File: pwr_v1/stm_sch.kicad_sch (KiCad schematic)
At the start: 2 parts, among them CN11 Conn_02x36_Odd_Even, CN12 Conn_02x36_Odd_Even

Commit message: Schematic updated
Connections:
- net KICKER_DISCHARGE: now also CN12.25 (Pin_25)
- net MOTOR1_ENCODER: now also CN11.9 (Pin_9)
- net MOTOR1_REVERSE: now also CN12.17 (Pin_17)
- net MOTOR2_BREAK: now also CN12.41 (Pin_41)
- net MOTOR3_BREAK: now also CN12.43 (Pin_43)
- net MOTOR3_ENCODER: now also CN12.35 (Pin_35)
- net MOTOR4_REVERSE: now also CN12.47 (Pin_47)
- net SPI_CS_CONF: no longer names the net of CN11.45 (Pin_45)
- net SPI_CS_OUTPUT: no longer names the net of CN11.40 (Pin_40)
- net SPI_CS_RESET: no longer names the net of CN11.39 (Pin_39)
- net SPI_CS_SHIFT: no longer names the net of CN11.43 (Pin_43)
- net SPI_CS_STORE: no longer names the net of CN11.41 (Pin_41)
- net SPI_MOSI: no longer names the net of CN12.29 (Pin_29)
- no-connect marks 112 -> 118
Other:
- moved on the sheet: CN11, CN12

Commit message: Schematic and layout updated
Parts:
- CN11, CN12: footprint (none) -> Connector_PinHeader_2.54mm:PinHeader_2x36_P2.54mm_Vertical_SMD
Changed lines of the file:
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@@
 			)
 		)
-		(property "Footprint" ""
+		(property "Footprint" "Connector_PinHeader_2.54mm:PinHeader_2x36_P2.54mm_Vertical_SMD"
 			(at 91.44 92.71 0)
 			(effects
@@
 			)
 		)
-		(property "Footprint" ""
+		(property "Footprint" "Connector_PinHeader_2.54mm:PinHeader_2x36_P2.54mm_Vertical_SMD"
 			(at 190.5 95.25 0)
 			(effects

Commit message: Schematic updated
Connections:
- net GND: now reaches CN11.20 (Pin_20)
- net 5V: now reaches CN11.6 (Pin_6)
- net MOSI: now reaches CN12.15 (Pin_15)
- net NRF_CSN renamed CS_NRF
- net NRF_MISO renamed MISO
- net NRF_SCK renamed SCK
- no-connect marks 118 -> 115
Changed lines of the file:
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@@
-	)
-	(no_connect
-		(at 99.06 54.61)
 	)
 	(no_connect
@@
 	)
 	(no_connect
-		(at 185.42 69.85)
-	)
-	(no_connect
 		(at 86.36 69.85)
 	)
@@
 	)
 	(no_connect
-		(at 99.06 72.39)
-	)
-	(no_connect
 		(at 185.42 85.09)
 	)
@@
 	(wire
 		(pts
+			(xy 99.06 72.39) (xy 105.918 72.39)
+		)
+		(stroke
+			(width 0)
+			(type default)
+		)
+	)
+	(wire
+		(pts
 			(xy 185.42 95.25) (xy 172.72 95.25)
 		)
@@
 	(wire
 		(pts
+			(xy 172.466 69.85) (xy 185.42 69.85)
+		)
+		(stroke
+			(width 0)
+			(type default)
+		)
+	)
+	(wire
+		(pts
 			(xy 198.12 85.09) (xy 210.82 85.09)
 		)
@@
 		(pts
 			(xy 99.06 105.41) (xy 111.76 105.41)
+		)
+		(stroke
+			(width 0)
+			(type default)
+		)
+	)
+	(wire
+		(pts
+			(xy 99.06 54.61) (xy 105.918 54.61)
 		)
 		(stroke
@@
 		)
 	)
+	(hierarchical_label "5V"
+		(shape input)
+		(at 105.918 54.61 0)
+		(fields_autoplaced yes)
+		(effects
+			(font
+				(size 1.27 1.27)
+			)
+			(justify left)
+		)
+	)
 	(hierarchical_label "MOTOR2_PWM"
 		(shape input)
@@
 		)
 	)
-	(hierarchical_label "NRF_CSN"
+	(hierarchical_label "CS_NRF"
 		(shape input)
 		(at 172.72 54.61 180)
@@
 		)
 	)
+	(hierarchical_label "GND"
+		(shape input)
+		(at 105.918 72.39 0)
+		(fields_autoplaced yes)
+		(effects
+			(font
+				(size 1.27 1.27)
+			)
+			(justify left)
+		)
+	)
 	(hierarchical_label "BTN_USER"
 		(shape input)
@@
 		)
 	)
-	(hierarchical_label "NRF_MISO"
+	(hierarchical_label "MISO"
 		(shape input)
 		(at 172.72 67.31 180)
@@
 		)
 	)
-	(hierarchical_label "NRF_SCK"
+	(hierarchical_label "SCK"
 		(shape input)
 		(at 172.72 64.77 180)
 		(fields_autoplaced yes)
 		(effects
+			(font
+				(size 1.27 1.27)
+			)
+			(justify right)
+		)
+	)
+	(hierarchical_label "MOSI"
+		(shape input)
+		(at 172.466 69.85 180)
+		(fields_autoplaced yes)
+		(effects

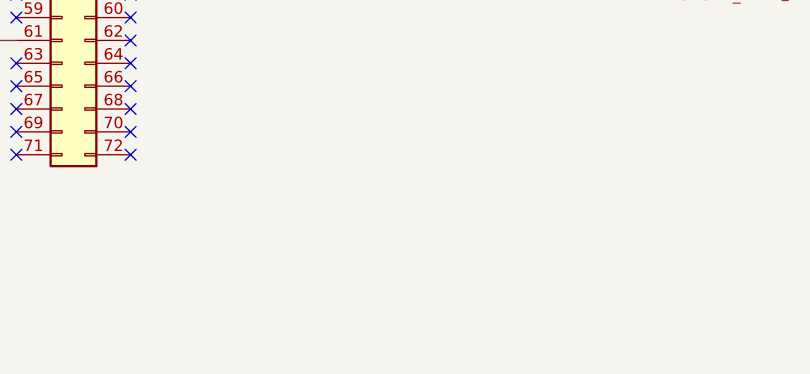
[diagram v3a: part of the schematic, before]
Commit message: Sch and Layout updated; Added batt sup ckt, placed and routed all motor drivers.
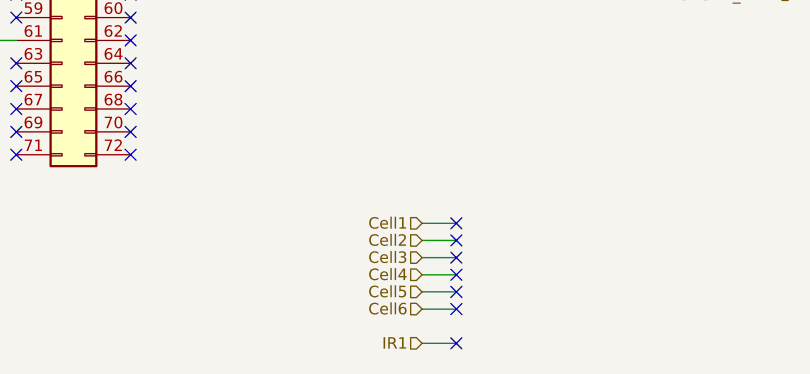
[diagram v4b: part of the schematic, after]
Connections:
- no-connect marks 115 -> 122
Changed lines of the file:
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@@
+	)
+	(no_connect
+		(at 135.255 146.05)
 	)
 	(no_connect
@@
 	)
 	(no_connect
+		(at 135.255 151.765)
+	)
+	(no_connect
 		(at 86.36 87.63)
 	)
@@
 	)
 	(no_connect
+		(at 135.255 147.955)
+	)
+	(no_connect
 		(at 99.06 95.25)
 	)
@@
 	)
 	(no_connect
+		(at 135.255 149.86)
+	)
+	(no_connect
 		(at 185.42 138.43)
 	)
@@
 	)
 	(no_connect
+		(at 135.255 155.575)
+	)
+	(no_connect
 		(at 198.12 128.27)
 	)
@@
 	)
 	(no_connect
+		(at 135.255 159.385)
+	)
+	(no_connect
 		(at 198.12 64.77)
 	)
@@
 	)
 	(no_connect
+		(at 135.255 153.67)
+	)
+	(no_connect
 		(at 198.12 115.57)
 	)
@@
 	(wire
 		(pts
+			(xy 131.445 151.765) (xy 135.255 151.765)
+		)
+		(stroke
+			(width 0)
+			(type default)
+		)
+	)
+	(wire
+		(pts
 			(xy 185.42 67.31) (xy 172.72 67.31)
 		)
@@
 	(wire
 		(pts
+			(xy 131.445 147.955) (xy 135.255 147.955)
+		)
+		(stroke
+			(width 0)
+			(type default)
+		)
+	)
+	(wire
+		(pts
 			(xy 185.42 72.39) (xy 172.72 72.39)
 		)
@@
 	(wire
 		(pts
+			(xy 131.445 159.385) (xy 135.255 159.385)
+		)
+		(stroke
+			(width 0)
+			(type default)
+		)
+	)
+	(wire
+		(pts
 			(xy 99.06 54.61) (xy 105.918 54.61)
 		)
@@
 	(wire
 		(pts
+			(xy 131.445 153.67) (xy 135.255 153.67)
+		)
+		(stroke
+			(width 0)
+			(type default)
+		)
+	)
+	(wire
+		(pts
 			(xy 185.42 115.57) (xy 172.72 115.57)
 		)
@@
 	(wire
 		(pts
+			(xy 131.445 149.86) (xy 135.255 149.86)
+		)
+		(stroke
+			(width 0)
+			(type default)
+		)
+	)
+	(wire
+		(pts
 			(xy 185.42 102.87) (xy 172.72 102.87)
 		)
@@
 	(wire
 		(pts
+			(xy 131.445 155.575) (xy 135.255 155.575)
+		)
+		(stroke
+			(width 0)
+			(type default)
+		)
+	)
+	(wire
+		(pts
 			(xy 185.42 82.55) (xy 172.72 82.55)
 		)
@@
 		(pts
 			(xy 86.36 125.73) (xy 73.66 125.73)
+		)
+		(stroke
+			(width 0)
+			(type default)
+		)
+	)
+	(wire
+		(pts
+			(xy 131.445 146.05) (xy 135.255 146.05)
 		)
 		(stroke
@@
 		)
 	)
+	(hierarchical_label "Cell6"
+		(shape input)
+		(at 131.445 155.575 180)
+		(fields_autoplaced yes)
+		(effects
+			(font
+				(size 1.27 1.27)
+			)
+			(justify right)
+		)
+	)
 	(hierarchical_label "5V"
 		(shape input)
@@
 		)
 	)
+	(hierarchical_label "Cell1"
+		(shape input)
+		(at 131.445 146.05 180)
+		(fields_autoplaced yes)
+		(effects
+			(font
+				(size 1.27 1.27)
+			)
+			(justify right)
+		)
+	)
 	(hierarchical_label "LED_YELLOW"
 		(shape input)
@@
 		)
 	)
+	(hierarchical_label "Cell3"
+		(shape input)
+		(at 131.445 149.86 180)
+		(fields_autoplaced yes)
+		(effects
+			(font
+				(size 1.27 1.27)
+			)
+			(justify right)
+		)
+	)
 	(hierarchical_label "GND"
 		(shape input)
@@
 		)
 	)
+	(hierarchical_label "Cell5"
+		(shape input)
+		(at 131.445 153.67 180)
+		(fields_autoplaced yes)
+		(effects
+			(font
+				(size 1.27 1.27)
+			)
+			(justify right)
+		)
+	)
+	(hierarchical_label "IR1"
+		(shape input)
+		(at 131.445 159.385 180)
+		(fields_autoplaced yes)
+		(effects
+			(font
+				(size 1.27 1.27)
+			)
+			(justify right)
+		)
+	)
 	(hierarchical_label "MOTOR4_REVERSE"
 		(shape input)
@@
 		(fields_autoplaced yes)
 		(effects
+			(font
+				(size 1.27 1.27)
+			)
+			(justify right)
+		)
+	)
+	(hierarchical_label "Cell4"
+		(shape input)
+		(at 131.445 151.765 180)
+		(fields_autoplaced yes)
+		(effects
+			(font
+				(size 1.27 1.27)
+			)
+			(justify right)
+		)
+	)
+	(hierarchical_label "Cell2"
+		(shape input)
+		(at 131.445 147.955 180)
+		(fields_autoplaced yes)
+		(effects

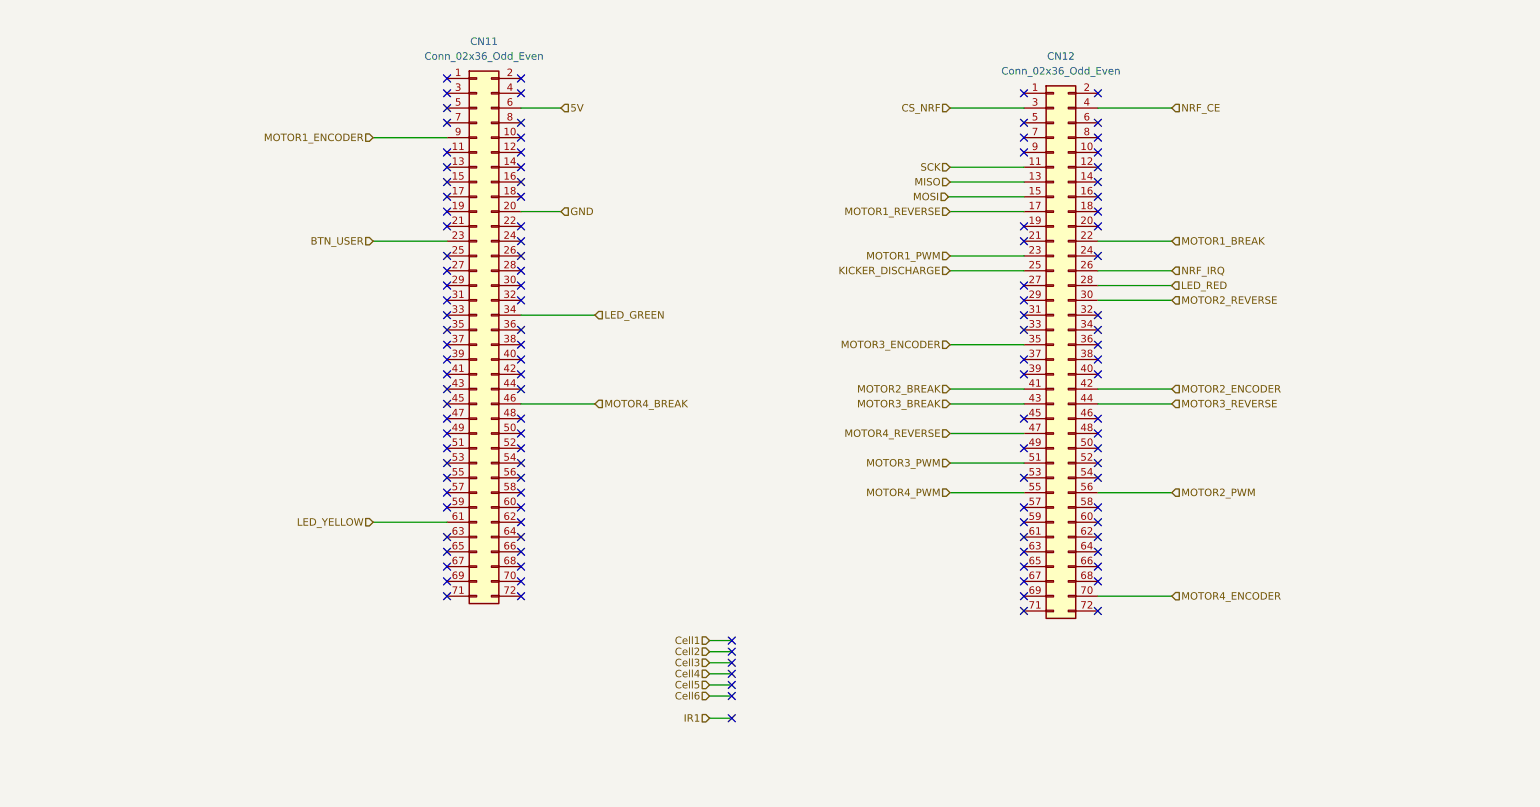
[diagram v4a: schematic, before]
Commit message: Schematic updated; Layout updated; STM PinMappings file added
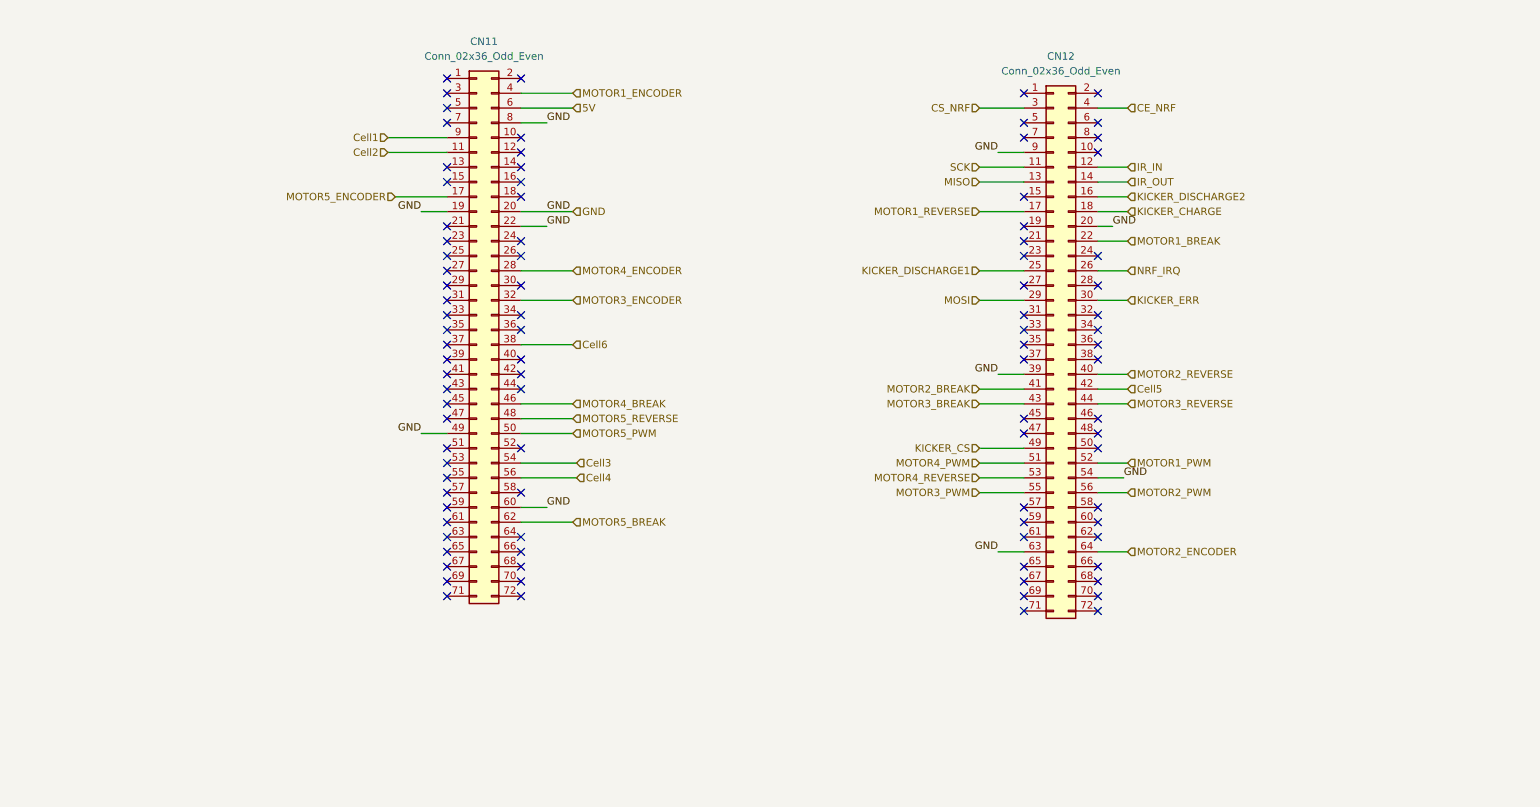
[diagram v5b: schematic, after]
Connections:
- net Cell1: now also CN11.9 (Pin_9)
- net Cell2: now also CN11.11 (Pin_11)
- net Cell3: now also CN11.54 (Pin_54)
- net Cell4: now also CN11.56 (Pin_56)
- net Cell5: now also CN12.42 (Pin_42)
- net Cell6: now also CN11.38 (Pin_38)
- net GND: now also CN11.19 (Pin_19), CN11.22 (Pin_22), CN11.49 (Pin_49), CN11.60 (Pin_60), CN11.8 (Pin_8), CN12.20 (Pin_20), CN12.39 (Pin_39), CN12.54 (Pin_54), CN12.63 (Pin_63), CN12.9 (Pin_9)
- net MOSI: now also CN12.29 (Pin_29); no longer CN12.15 (Pin_15)
- net MOTOR1_ENCODER: now also CN11.4 (Pin_4); no longer CN11.9 (Pin_9)
- net MOTOR1_PWM: now also CN12.52 (Pin_52); no longer CN12.23 (Pin_23)
- net MOTOR2_ENCODER: now also CN12.64 (Pin_64); no longer CN12.42 (Pin_42)
- net MOTOR2_REVERSE: now also CN12.40 (Pin_40); no longer CN12.30 (Pin_30)
- net MOTOR3_ENCODER: now also CN11.32 (Pin_32); no longer CN12.35 (Pin_35)
- net MOTOR3_PWM: now also CN12.55 (Pin_55); no longer CN12.51 (Pin_51)
- net MOTOR4_ENCODER: now also CN11.28 (Pin_28); no longer CN12.70 (Pin_70)
- net MOTOR4_PWM: now also CN12.51 (Pin_51); no longer CN12.55 (Pin_55)
- net MOTOR4_REVERSE: now also CN12.53 (Pin_53); no longer CN12.47 (Pin_47)
- net MOTOR5_ENCODER: now reaches CN11.17 (Pin_17)
- net MOTOR5_REVERSE: now reaches CN11.48 (Pin_48)
- net MOTOR5_PWM: now reaches CN11.50 (Pin_50)
- net MOTOR5_BREAK: now reaches CN11.62 (Pin_62)
- net IR_IN: now reaches CN12.12 (Pin_12)
- net IR_OUT: now reaches CN12.14 (Pin_14)
- net KICKER_DISCHARGE2: now reaches CN12.16 (Pin_16)
- net KICKER_CHARGE: now reaches CN12.18 (Pin_18)
- net KICKER_CS: now reaches CN12.49 (Pin_49)
- net BTN_USER: no longer names the net of CN11.23 (Pin_23)
- net KICKER_DISCHARGE renamed KICKER_DISCHARGE1
- net LED_GREEN: no longer names the net of CN11.34 (Pin_34)
- net LED_RED: no longer names the net of CN12.28 (Pin_28)
- net LED_YELLOW: no longer names the net of CN11.61 (Pin_61)
- net NRF_CE renamed CE_NRF
- new net KICKER_ERR: CN12.30 (Pin_30)
- no-connect marks 122 -> 93

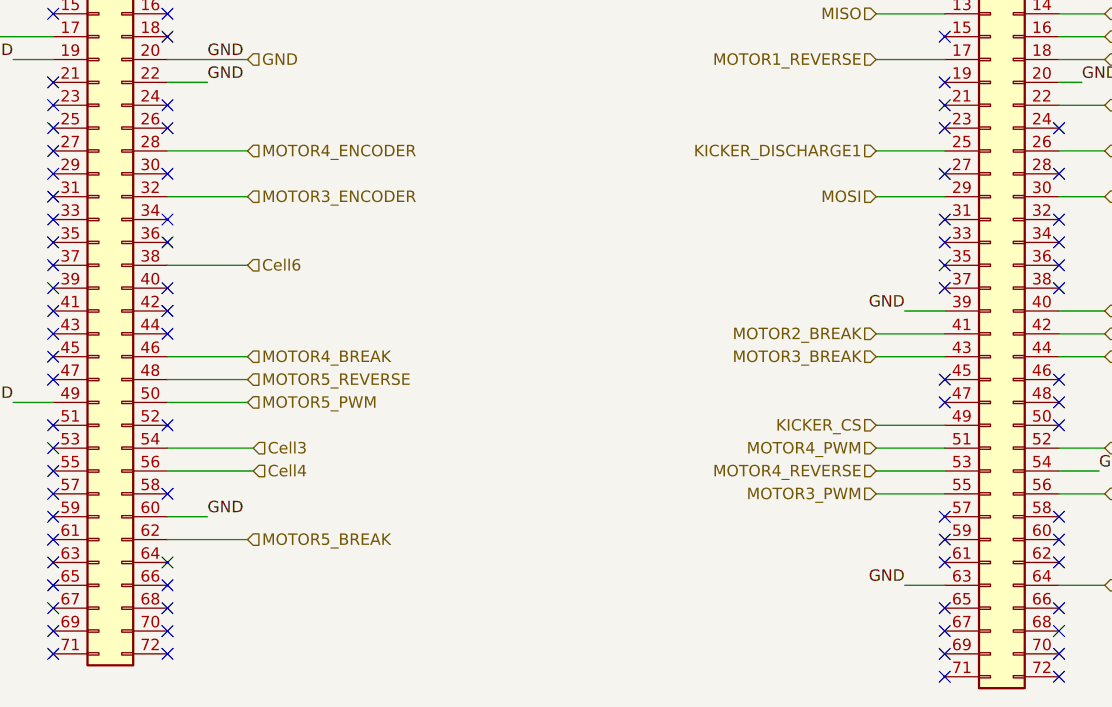
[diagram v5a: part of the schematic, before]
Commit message: Schematic and layout updated; Layout placement and routing completed
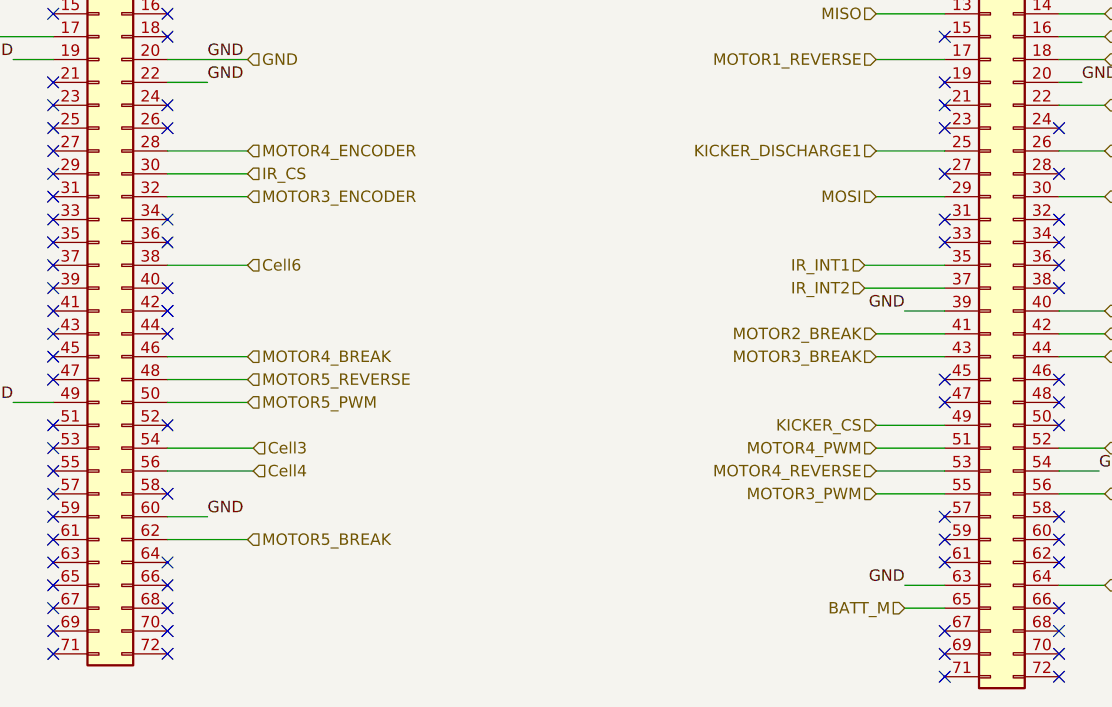
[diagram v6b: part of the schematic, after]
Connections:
- net IR_CS: now reaches CN11.30 (Pin_30)
- net IR_INT1: now reaches CN12.35 (Pin_35)
- net IR_INT2: now reaches CN12.37 (Pin_37)
- net BATT_M: now reaches CN12.65 (Pin_65)
- no-connect marks 93 -> 89
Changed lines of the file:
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@@
-	)
-	(no_connect
-		(at 185.42 133.35)
 	)
 	(no_connect
@@
 	)
 	(no_connect
-		(at 185.42 95.25)
-	)
-	(no_connect
 		(at 198.12 52.07)
 	)
@@
 	)
 	(no_connect
-		(at 99.06 85.09)
-	)
-	(no_connect
 		(at 185.42 77.47)
 	)
@@
 	)
 	(no_connect
-		(at 185.42 97.79)
-	)
-	(no_connect
 		(at 86.36 115.57)
 	)
@@
 	(wire
 		(pts
+			(xy 107.95 85.09) (xy 99.06 85.09)
+		)
+		(stroke
+			(width 0)
+			(type default)
+		)
+	)
+	(wire
+		(pts
 			(xy 177.8 105.41) (xy 185.42 105.41)
 		)
@@
 	(wire
 		(pts
+			(xy 176.53 95.25) (xy 185.42 95.25)
+		)
+		(stroke
+			(width 0)
+			(type default)
+		)
+	)
+	(wire
+		(pts
 			(xy 203.2 120.65) (xy 198.12 120.65)
 		)
@@
 	(wire
 		(pts
+			(xy 180.975 133.35) (xy 185.42 133.35)
+		)
+		(stroke
+			(width 0)
+			(type default)
+		)
+	)
+	(wire
+		(pts
 			(xy 107.95 82.55) (xy 99.06 82.55)
 		)
@@
 		(pts
 			(xy 99.06 72.39) (xy 107.95 72.39)
+		)
+		(stroke
+			(width 0)
+			(type default)
+		)
+	)
+	(wire
+		(pts
+			(xy 176.53 97.79) (xy 185.42 97.79)
 		)
 		(stroke
@@
 		)
 	)
+	(hierarchical_label "IR_INT1"
+		(shape input)
+		(at 176.53 95.25 180)
+		(fields_autoplaced yes)
+		(effects
+			(font
+				(size 1.27 1.27)
+			)
+			(justify right)
+		)
+	)
 	(hierarchical_label "MOTOR5_REVERSE"
 		(shape input)
@@
 		)
 	)
+	(hierarchical_label "IR_CS"
+		(shape input)
+		(at 107.95 85.09 0)
+		(fields_autoplaced yes)
+		(effects
+			(font
+				(size 1.27 1.27)
+			)
+			(justify left)
+		)
+	)
 	(hierarchical_label "SCK"
 		(shape input)
@@
 		(fields_autoplaced yes)
 		(effects
+			(font
+				(size 1.27 1.27)
+			)
+			(justify right)
+		)
+	)
+	(hierarchical_label "IR_INT2"
+		(shape input)
+		(at 176.53 97.79 180)
+		(fields_autoplaced yes)
+		(effects
+			(font
+				(size 1.27 1.27)
+			)
+			(justify right)
+		)
+	)
+	(hierarchical_label "BATT_M"
+		(shape input)
+		(at 180.975 133.35 180)
+		(fields_autoplaced yes)
+		(effects
